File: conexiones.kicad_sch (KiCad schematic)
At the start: 5 parts, among them J1 Conn_01x06, J2 Conn_01x06, J3 Conn_01x06, J4 AudioJack3_Switch, J5 AudioJack3_Switch

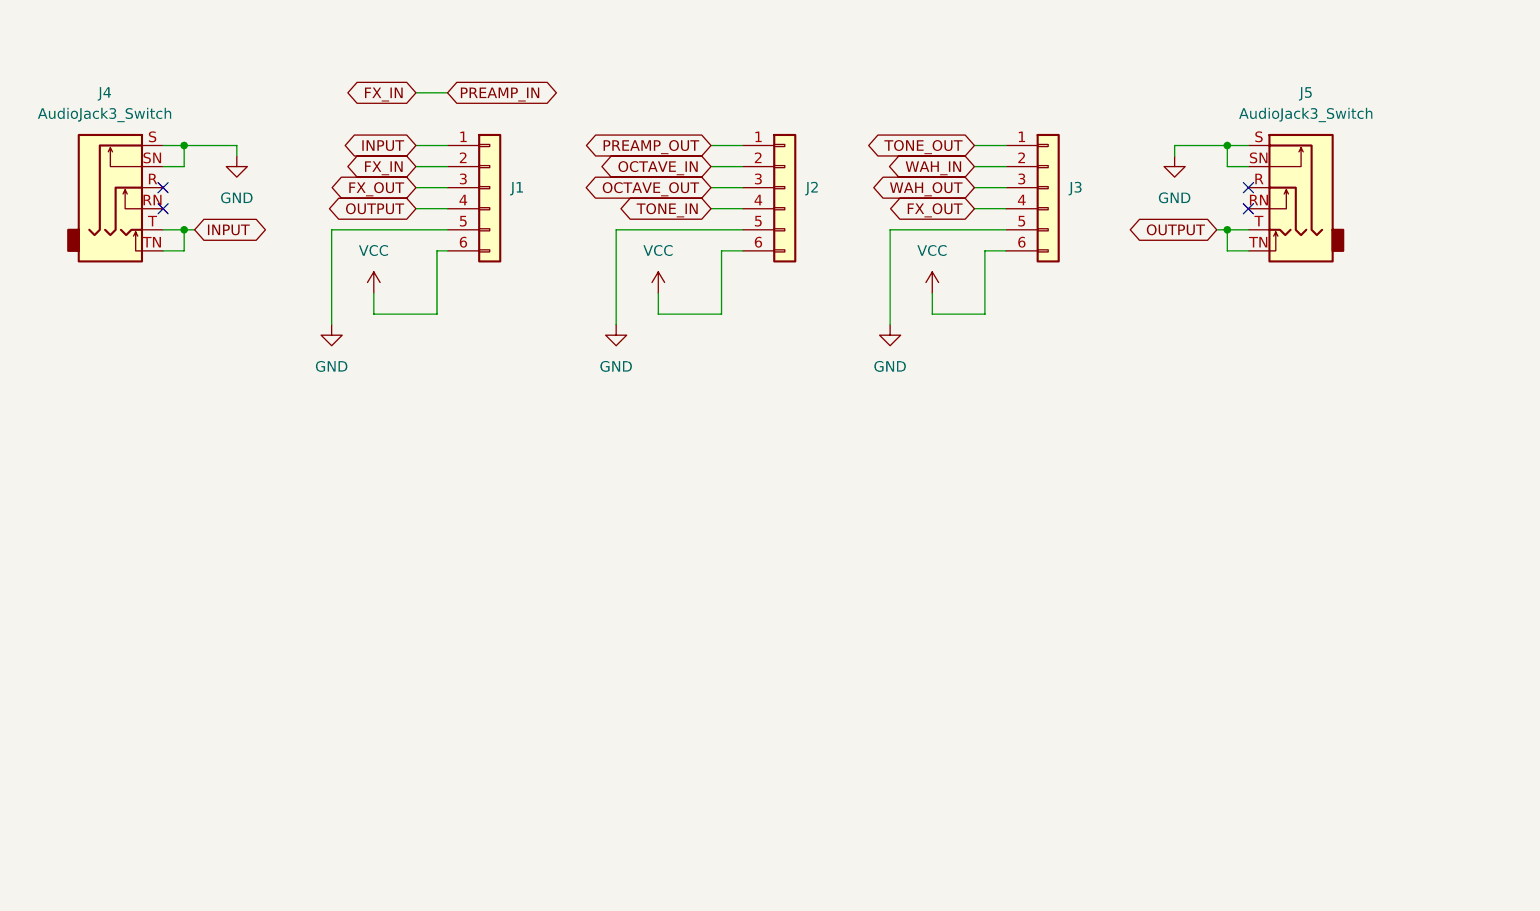
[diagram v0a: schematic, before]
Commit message: Actualización de esquemáticos
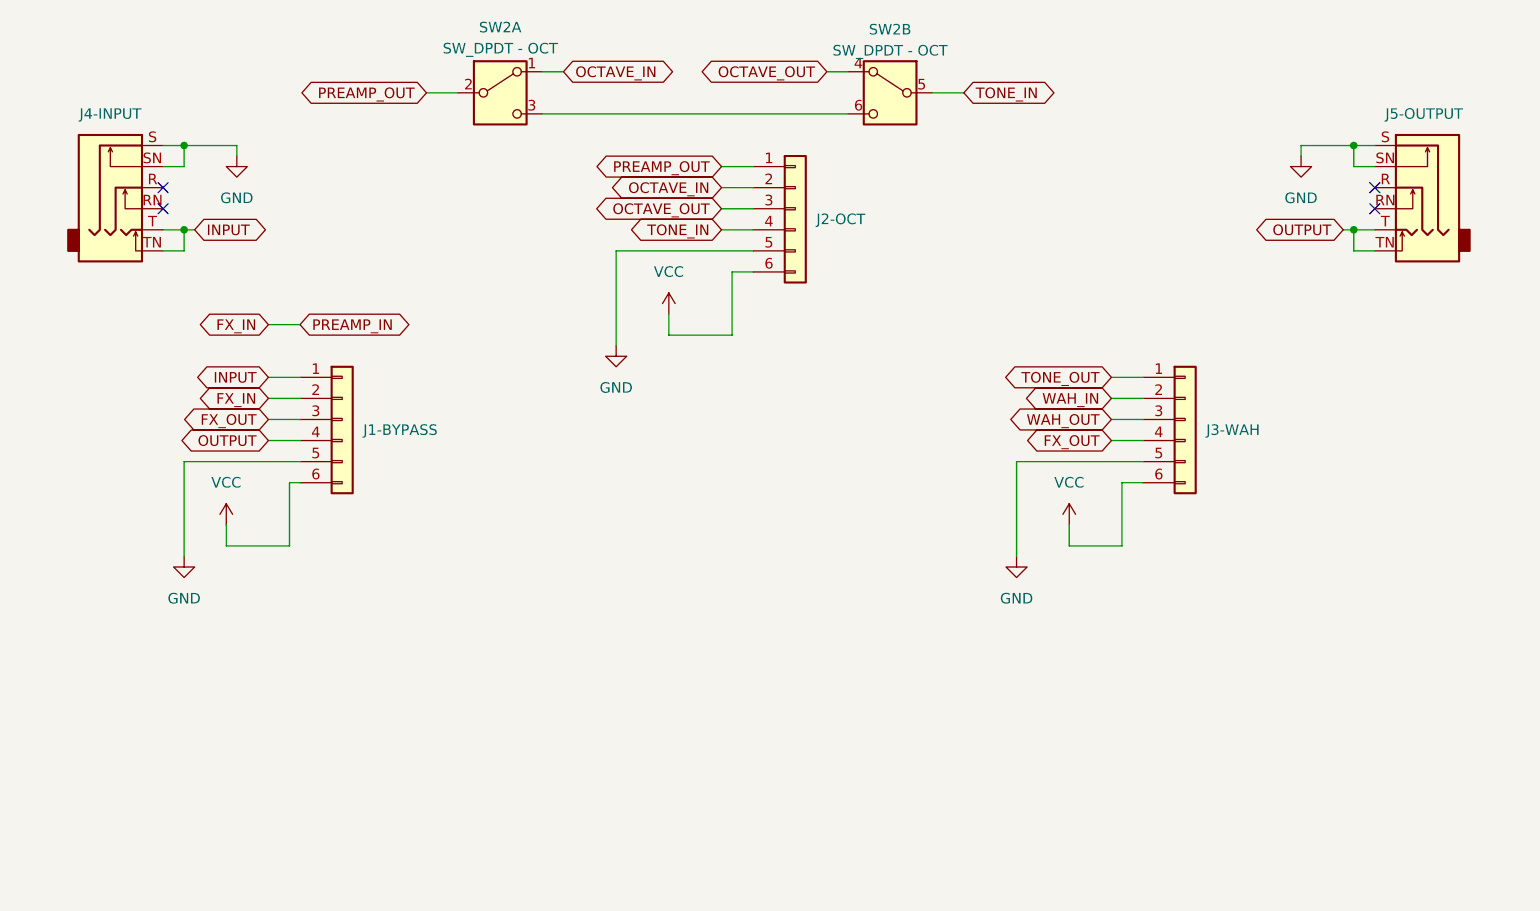
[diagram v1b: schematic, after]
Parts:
- added SW2: SW_DPDT - OCT, symbol Switch:SW_DPDT_x2
- renumbered J1 to J1-BYPASS, J2 to J2-OCT, J3 to J3-WAH, J4 to J4-INPUT, J5 to J5-OUTPUT
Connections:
- net OCTAVE_IN: now also SW2.1 (A)
- net OCTAVE_OUT: now also SW2.4 (A)
- net PREAMP_OUT: now also SW2.2 (B)
- net TONE_IN: now also SW2.5 (B)
- new net: SW2.3 (C), SW2.6 (C)
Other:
- moved on the sheet: J1-BYPASS, J2-OCT, J3-WAH, J5-OUTPUT

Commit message: Actualización esquemáticos
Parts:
- removed J2-OCT: Conn_01x06, Connector_PinHeader_2.54mm:PinHeader_1x06_P2.54mm_Vertical, symbol Connector_Generic:Conn_01x06
- added J5: EXP, Connector_Audio:Jack_6.35mm_Neutrik_NMJ6HCD3_Horizontal, symbol Connector_Audio:AudioJack3_Switch
- J1: renamed from J1-BYPASS; value Conn_01x06 -> BYPASS
- J2: renamed from J3-WAH; value Conn_01x06 -> WAH
- J3: renamed from J4-INPUT; value AudioJack3_Switch -> INPUT
- J4: renamed from J5-OUTPUT; value AudioJack3_Switch -> OUTPUT
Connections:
- net GND: now also J5.S
- net FX_IN renamed PREAMP_IN
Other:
- moved on the sheet: J1, J2, SW2A, SW2B

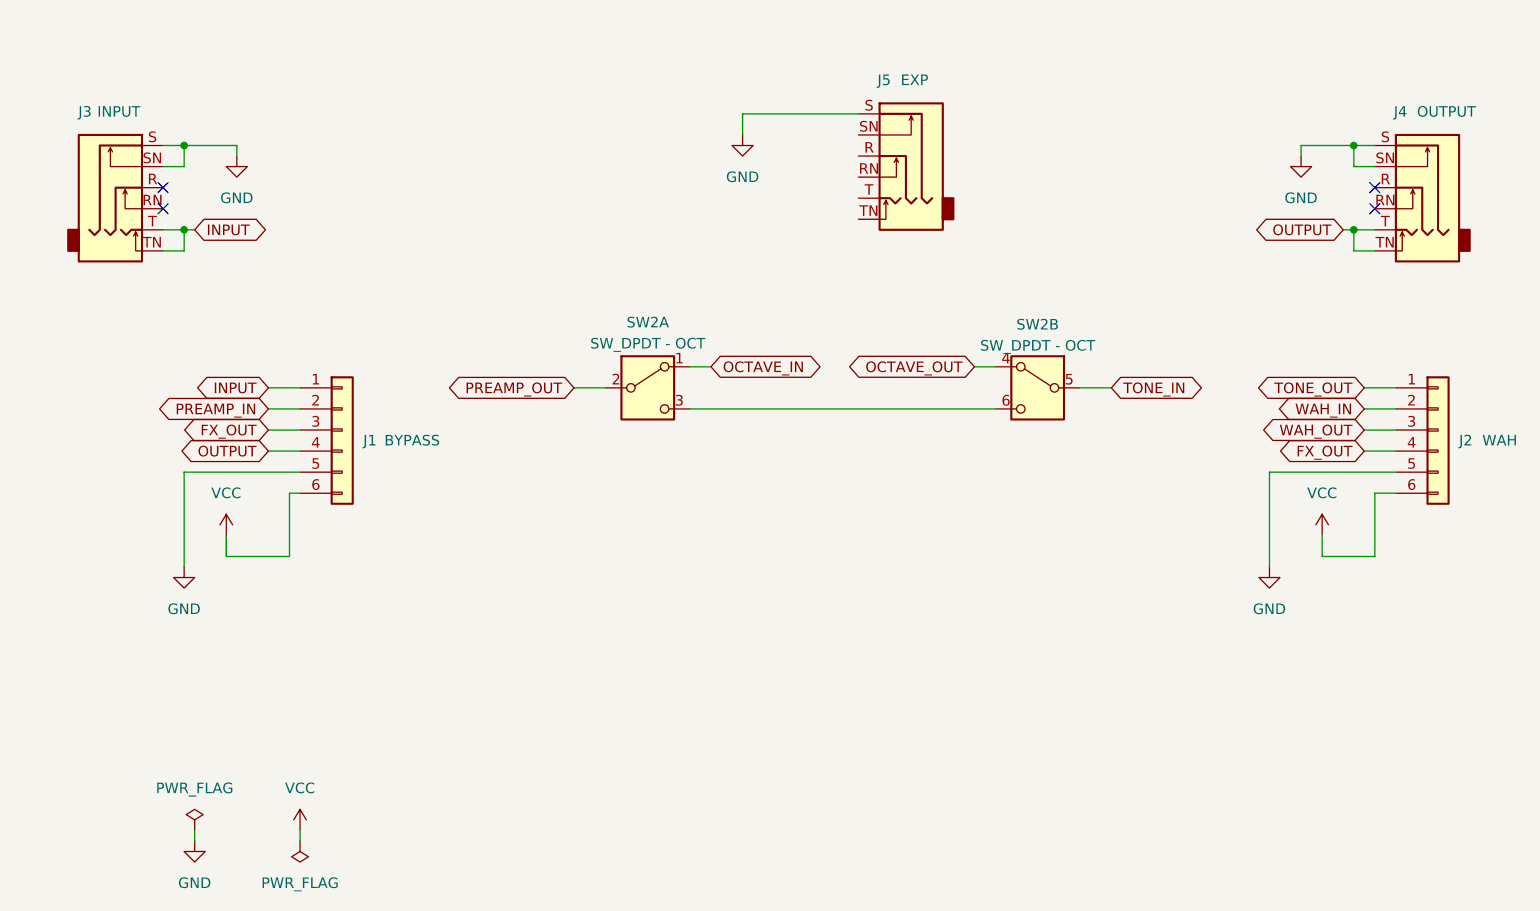
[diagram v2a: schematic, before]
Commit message: Asignación de huellas a componentes.
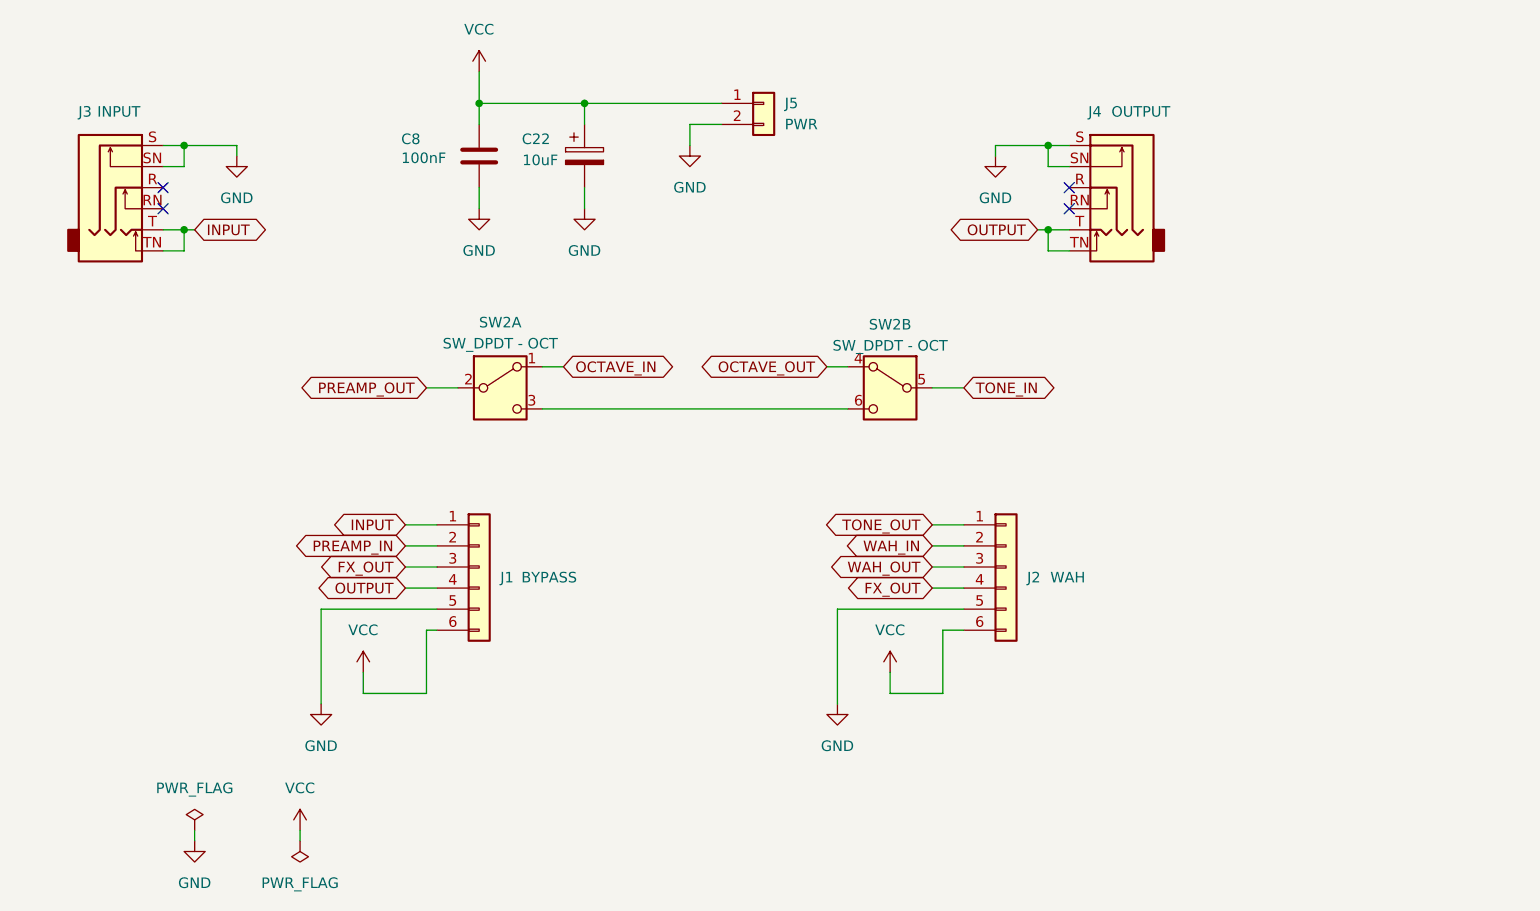
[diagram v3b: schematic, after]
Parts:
- removed J5: EXP, Connector_Audio:Jack_6.35mm_Neutrik_NMJ6HCD3_Horizontal, symbol Connector_Audio:AudioJack3_Switch
- added C22: 10uF, Capacitor_THT:CP_Radial_D5.0mm_P2.00mm, symbol Device:C_Polarized
- added C8: 100nF, Capacitor_THT:C_Disc_D5.1mm_W3.2mm_P5.00mm, symbol Device:C
- added J5: PWR, Connector_PinHeader_2.54mm:PinHeader_1x02_P2.54mm_Vertical, symbol Connector_Generic:Conn_01x02
- SW2: footprint (none) -> DIY_jorge:SW_DPDT
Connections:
- net GND: now also C22.2, C8.2, J5.2 (Pin_2)
- net VCC: now also C22.1, C8.1, J5.1 (Pin_1)
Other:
- moved on the sheet: J1, J2, J4, SW2A, SW2B

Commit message: Adctualización de PCB
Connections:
- net OCTAVE_IN: now also SW2.4 (A); no longer SW2.1 (A)
- net OCTAVE_OUT: now also SW2.1 (A); no longer SW2.4 (A)
- net PREAMP_OUT: now also SW2.5 (B); no longer SW2.2 (B)
- net TONE_IN: now also SW2.2 (B); no longer SW2.5 (B)
- new net: SW2.3 (C), SW2.6 (C)
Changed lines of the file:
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@@
 		(lib_id "Switch:SW_DPDT_x2")
 		(at 74.93 59.69 0)
-		(unit 1)
+		(unit 2)
 		(exclude_from_sim no)
 		(in_bom yes)
@@
 				(path "/6df9a4de-ce35-4607-9a42-d3c459c15494/d2a74948-ce64-4c01-a7b1-402e183435e4"
 					(reference "SW2")
-					(unit 1)
+					(unit 2)
 				)
 			)
@@
 		(at 121.92 59.69 0)
 		(mirror y)
-		(unit 2)
+		(unit 1)
 		(exclude_from_sim no)
 		(in_bom yes)
@@
 				(path "/6df9a4de-ce35-4607-9a42-d3c459c15494/d2a74948-ce64-4c01-a7b1-402e183435e4"
 					(reference "SW2")
-					(unit 2)
-				)
-			)
+					(unit 1)
+				)
+			)
